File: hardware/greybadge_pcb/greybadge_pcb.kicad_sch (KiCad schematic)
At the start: 94 parts, among them J1 Conn_02x05_Row_Letter_First, J2 Conn_02x05_Row_Letter_First, J3 Conn_02x05_Row_Letter_First, J4 Conn_02x05_Row_Letter_First, J5 78171-0002, SW1 SW_Push, SW2 SW_Push, SW3 SW_SPDT, SW4 SW_Push, SW5 SW_Push, SW6 SW_Push, SW7 SW_Push, SW8 SW_Push, U1 MT3608, U2 BQ24075, U3 TLV62568DBV, U4 TLV62568DBV, U5 TLV73325PDBV

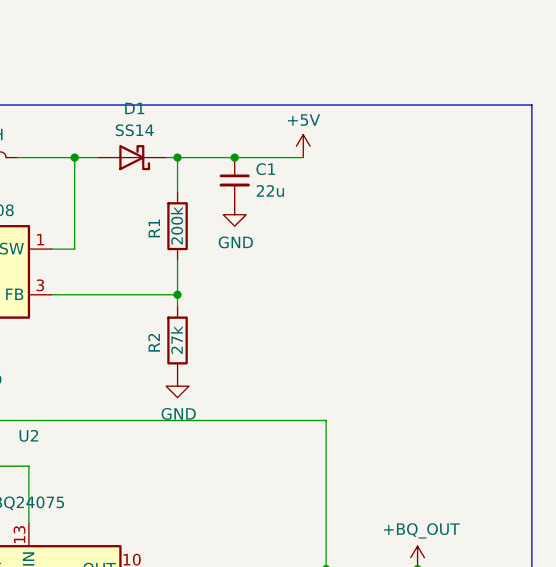
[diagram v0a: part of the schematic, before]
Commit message: feat: Add pads for AA batt
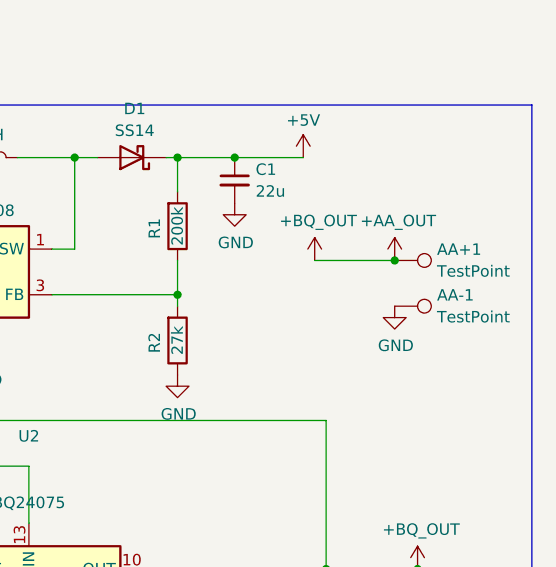
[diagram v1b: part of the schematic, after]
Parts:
- added AA+1, AA-1: TestPoint, TestPoint:TestPoint_Pad_D1.5mm, symbol Connector:TestPoint
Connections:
- net GND: now also AA-1.1
- net +BQ_OUT renamed +AA_OUT
- net +AA_OUT: now also AA+1.1

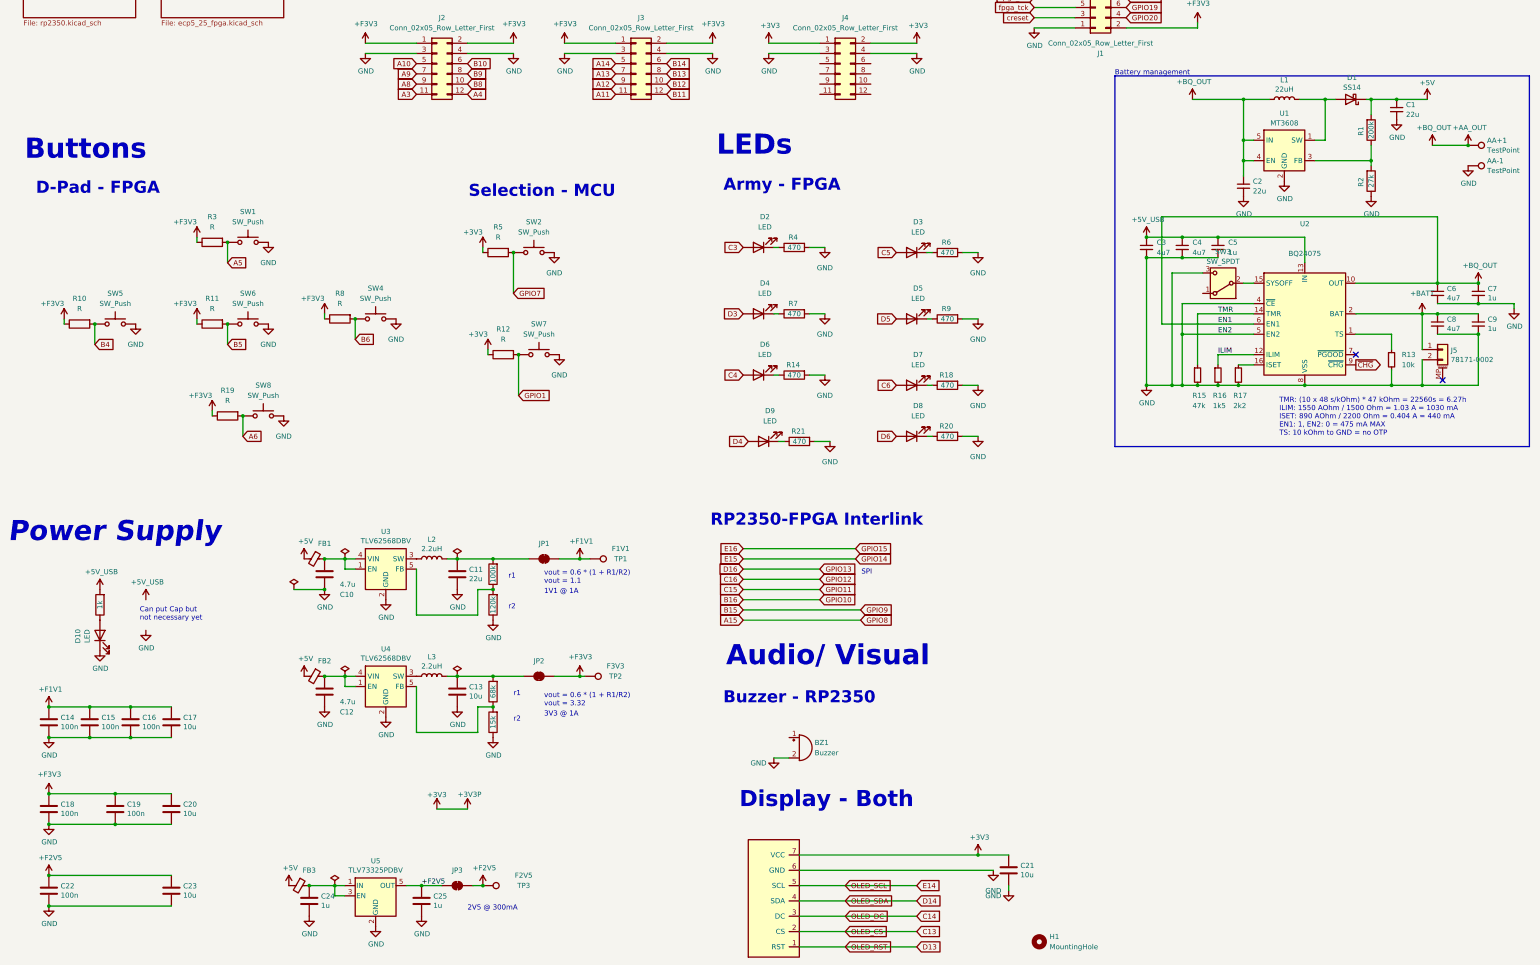
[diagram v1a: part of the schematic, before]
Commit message: Fix: Use 10k Ohm for R to fix backlight dimming on button press
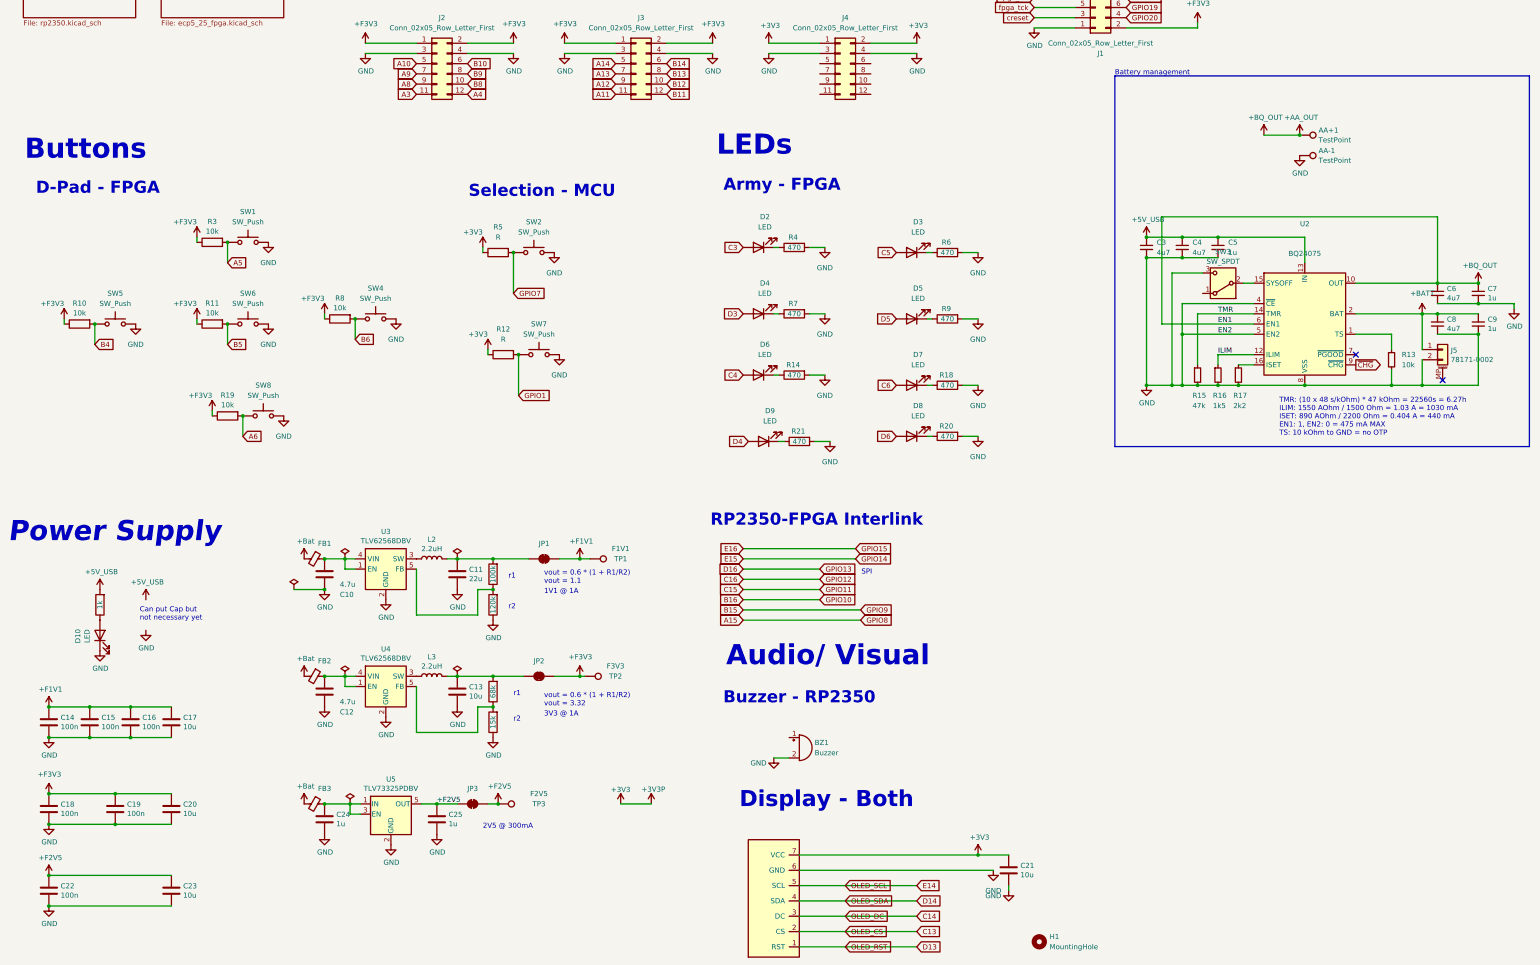
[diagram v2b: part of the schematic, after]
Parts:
- removed C1, C2: 22u, Capacitor_SMD:C_0402_1005Metric, symbol Device:C_Small
- removed D1: SS14, Diode_SMD:D_SMA, symbol Diode:SS14
- removed L1: 22uH, Inductor_SMD:L_Taiyo-Yuden_NR-40xx, symbol Device:L
- removed R1: 200k, Resistor_SMD:R_0603_1608Metric_Pad0.98x0.95mm_HandSolder, symbol Device:R
- removed R2: 27k, Resistor_SMD:R_0603_1608Metric_Pad0.98x0.95mm_HandSolder, symbol Device:R
- removed U1: MT3608, Package_TO_SOT_SMD:SOT-23-6, symbol Regulator_Switching:MT3608
- R10, R11, R19, R3, R8: value R -> 10k
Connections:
- net +5V renamed +Bat
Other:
- moved on the sheet: AA+1, AA-1, C24, C25, FB3, JP3, TP3, U5

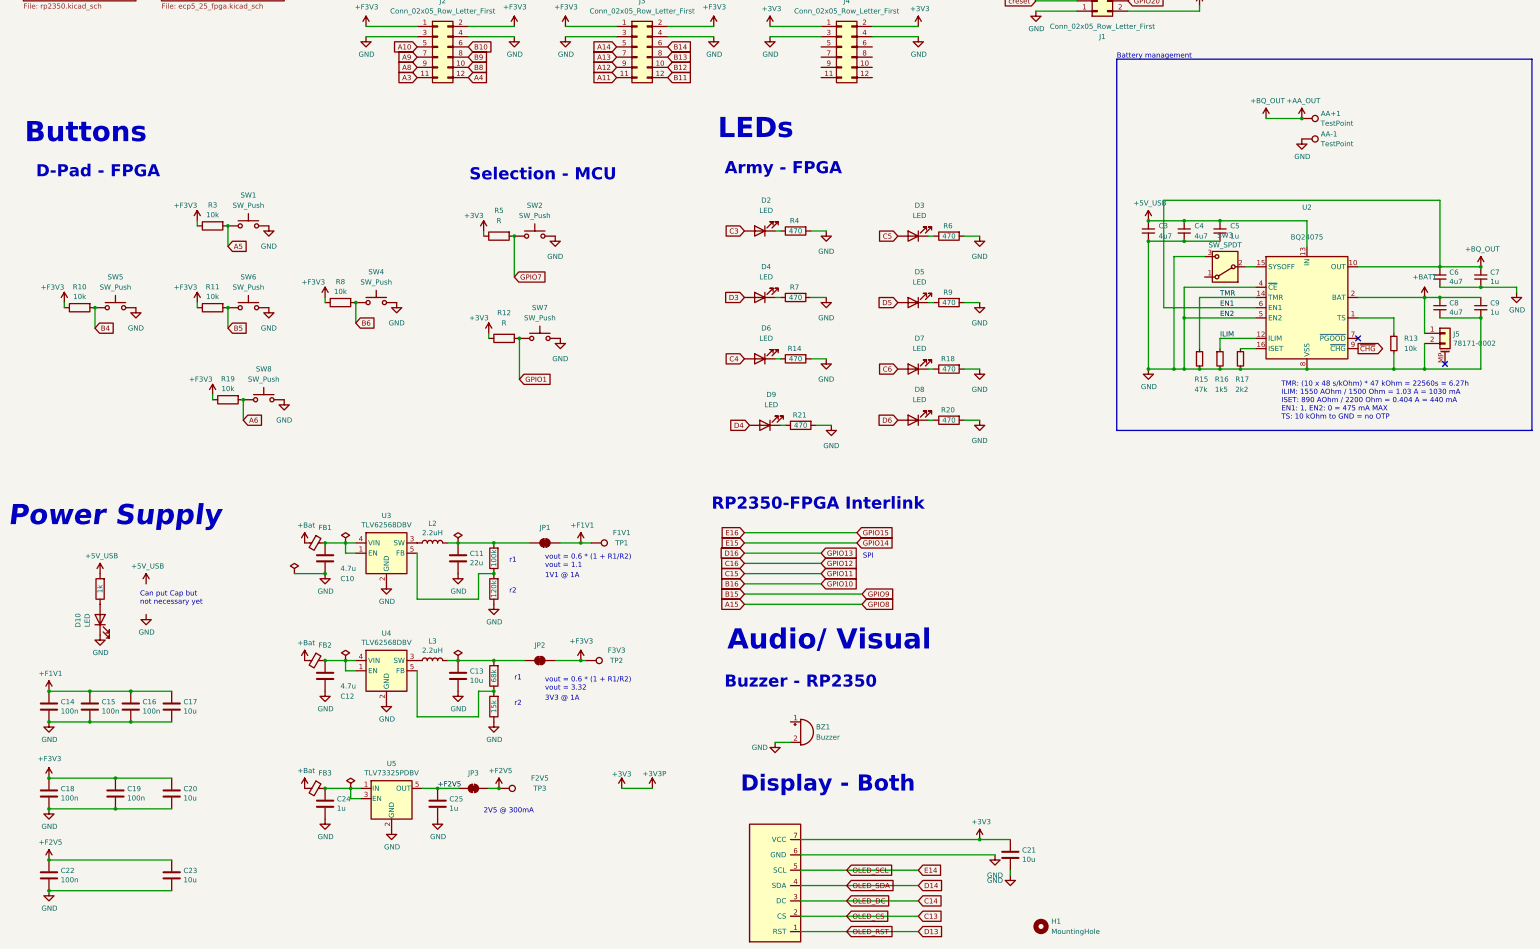
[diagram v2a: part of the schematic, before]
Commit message: Fix: battery/power and clean up silkscreen references
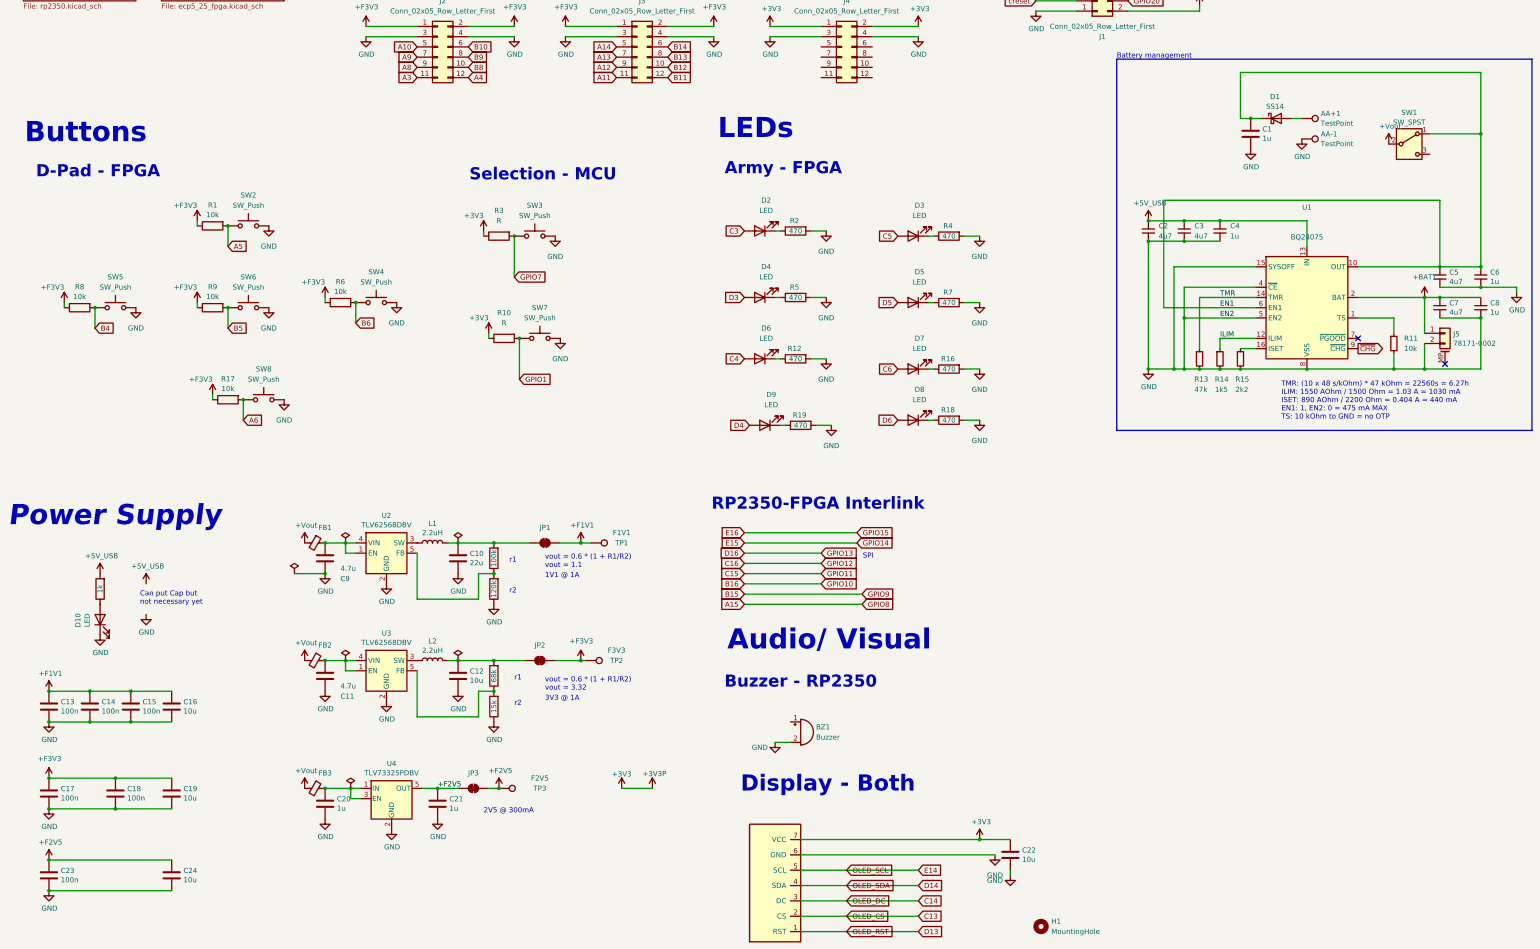
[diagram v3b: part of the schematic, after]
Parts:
- removed SW3: SW_SPDT, Button_Switch_SMD:SW_SPDT_CK_JS102011SAQN, symbol Switch:SW_SPDT
- added C1: 1u, Capacitor_SMD:C_0402_1005Metric, symbol Device:C
- added D1: SS14, Diode_SMD:D_SOD-123, symbol Diode:SS14
- added SW1: SW_SPST, Button_Switch_SMD:SW_SPDT_PCM12, symbol Switch:SW_SPDT
- renumbered C11 to C10, C12 to C11, C13 to C12, C14 to C13, C15 to C14, C16 to C15, C17 to C16, C18 to C17, C19 to C18, C20 to C19, C3 to C2, C24 to C20, C25 to C21, C21 to C22, C22 to C23, C23 to C24, C4 to C3, C5 to C4, C6 to C5, C7 to C6, C8 to C7, C9 to C8, C10 to C9, L2 to L1, L3 to L2, R3 to R1, R12 to R10, R13 to R11, R14 to R12, R15 to R13, R16 to R14, R17 to R15, R18 to R16, R19 to R17, R20 to R18, R21 to R19, R4 to R2, R22 to R20, R23 to R21, R24 to R22, R25 to R23, R26 to R24, R5 to R3, R6 to R4, R7 to R5, R8 to R6, R9 to R7, R10 to R8, R11 to R9, SW1 to SW2, SW2 to SW3, U2 to U1, U3 to U2, U4 to U3, U5 to U4
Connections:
- net GND: now also U1.15 (SYSOFF), C1.2
- net +AA_OUT renamed EN1
- net EN1: now also C1.1, D1.1 (K), SW1.1 (A); no longer AA+1.1
- net +Bat renamed +Vout
- net +Vout: now also SW1.2 (B)
- new net: AA+1.1, D1.2 (A)

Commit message: Add onboard oled (incomplete)
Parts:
- added C1: 0.1u, Capacitor_SMD:C_0603_1608Metric, symbol Device:C_Small
- added Q1: 2N7002, Package_TO_SOT_SMD:SOT-23, symbol Transistor_FET:2N7002
- added R1: 22, Resistor_SMD:R_0603_1608Metric, symbol Device:R_Small
- added R2: 10k, Resistor_SMD:R_0603_1608Metric, symbol Device:R_Small
- added R3: 1M, Resistor_SMD:R_0603_1608Metric, symbol Device:R_Small
- added U1: GC9A01_IPS_display, custom:GC9A01_IPS_display, symbol open-Smartwatch:GC9A01_IPS_display_SPI
- renumbered C9 to C10, C10 to C11, C11 to C12, C12 to C13, C13 to C14, C14 to C15, C15 to C16, C16 to C17, C17 to C18, C18 to C19, C1 to C2, C19 to C20, C20 to C21, C21 to C22, C22 to C23, C23 to C24, C24 to C25, C2 to C3, C3 to C4, C4 to C5, C5 to C6, C6 to C7, C7 to C8, C8 to C9, R7 to R10, R8 to R11, R9 to R12, R10 to R13, R12 to R14, R16 to R15, R17 to R16, R11 to R17, R13 to R20, R14 to R21, R15 to R22, R20 to R23, R21 to R24, R22 to R25, R23 to R26, R24 to R27, R1 to R4, R2 to R5, R3 to R6, R4 to R7, R5 to R8, R6 to R9, U1 to U2, U2 to U3, U3 to U4, U4 to U5
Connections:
- net C13: now also U1.8 (~{CS})
- net C14: now also U1.7 (D/C)
- net D13: now also U1.11 (~{RESET})
- net GND: now also C1.2, Q1.2 (S), R3.1, U1.1 (GND), U1.12 (GND), U1.5 (GND), U1.6 (GND)
- new net: R1.2, U1.3 (LEDA)
- new net: Q1.1 (G), R2.1, R3.2
- new net 3V3_2: C1.1, R1.1, U1.4 (VDD)
- new net LEDK: Q1.3 (D), U1.2 (LEDK)
- new net MOSI: U1.10 (SDI)
- new net PIN_LED: R2.2
- new net SCK: U1.9 (SCK)
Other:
- note added: "DISPLAY"
- moved on the sheet: AA+1, AA-1, C2, C3, C4, C5, C6, C7, C8, C9, D1, J5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
